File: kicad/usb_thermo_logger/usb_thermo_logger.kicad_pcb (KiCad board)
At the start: 2 copper layers, 80 x 61 mm, 50 parts, among them J1 690-005-299-043, J2 SWD, J3 RESET, J4 BOOT0, U1 STM32F070CBT6, U2 24AA02-OT, U3 MAX31855KASA, U4 MAX31855KASA, U5 PCA9531, U6 LD3985M33R_SOT23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

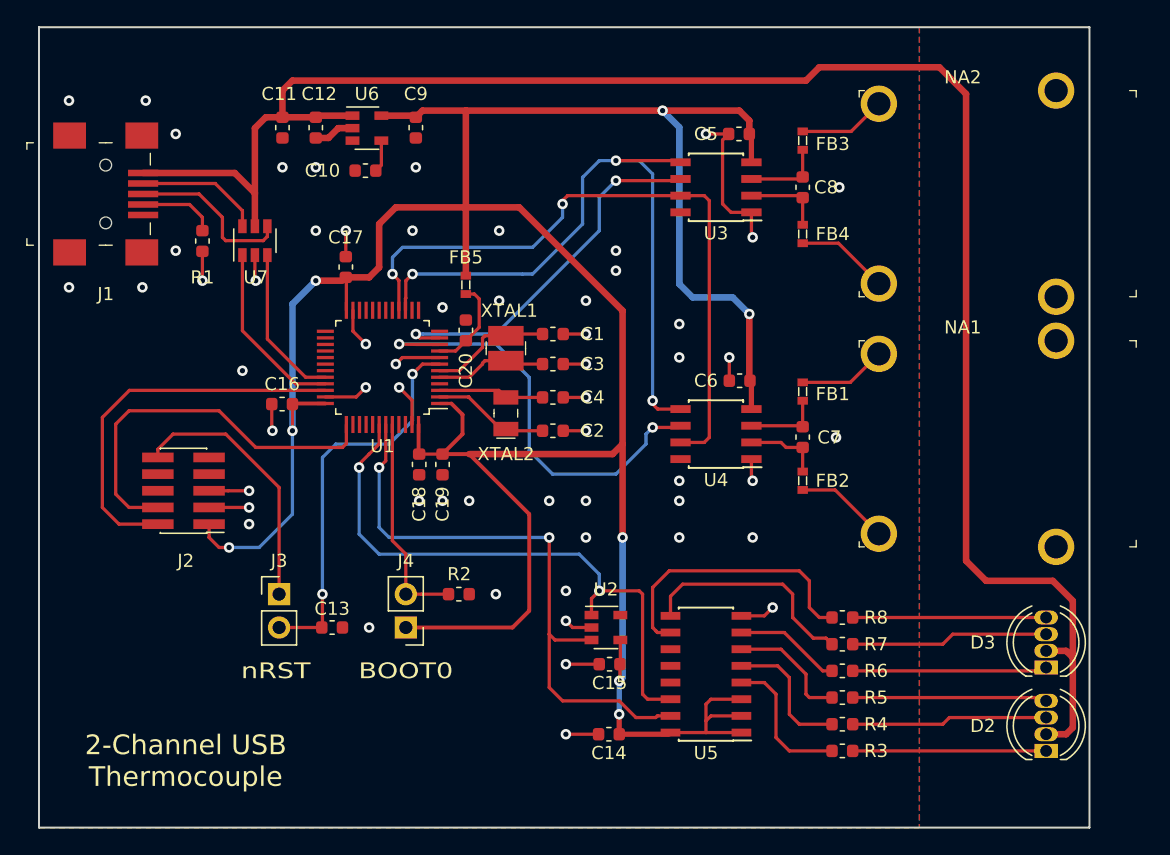
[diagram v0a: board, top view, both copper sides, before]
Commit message: LED display changes, added OpenSCAD
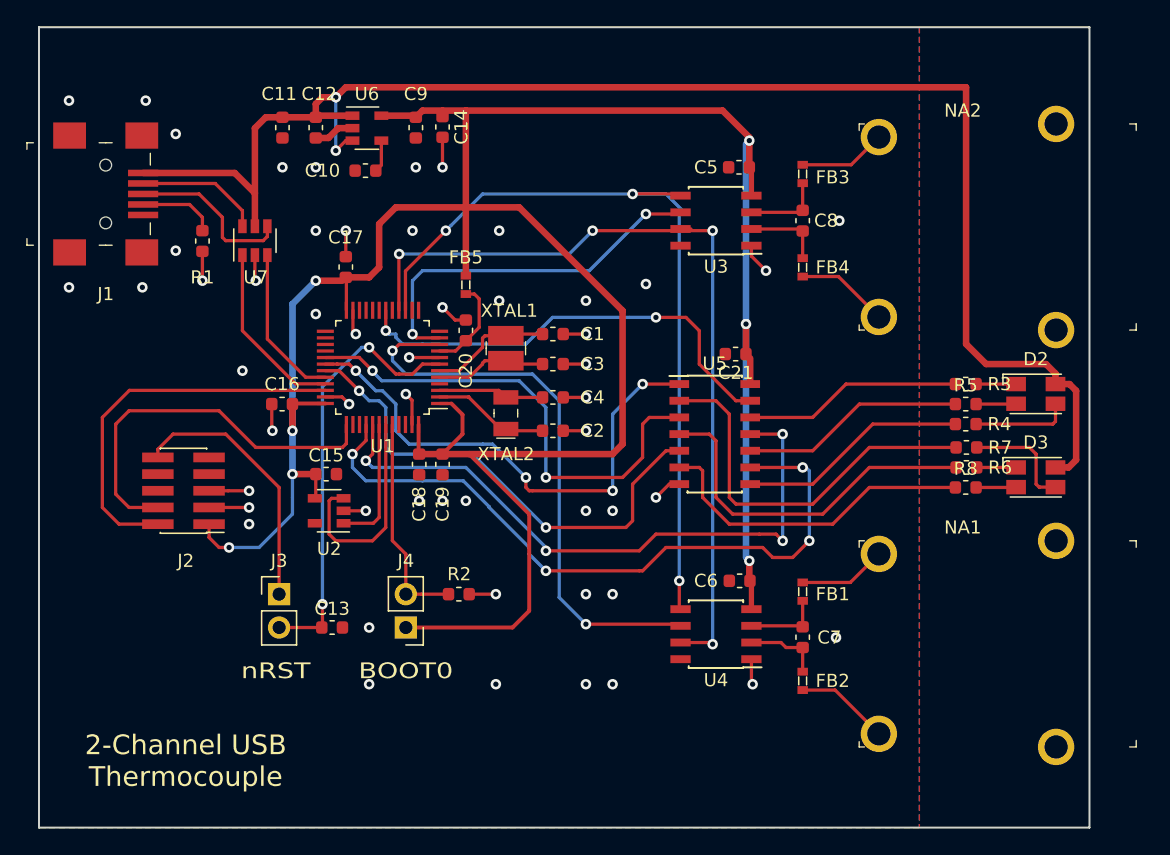
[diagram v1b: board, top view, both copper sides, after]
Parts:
- added C21: 100n, Capacitor_SMD:C_0603_1608Metric, F.Cu at (140.7, 88.4)
- D2, D3: footprint LED_THT:LED_D5.0mm-4_RGB -> LED_SMD:LED_Avago_PLCC4_3.2x2.8mm_CW
- R3, R6: value 560R -> 1k
- R4, R5, R7, R8: value 560R -> 2k2
- U5: value PCA9531 -> SN74LVC06ADR; footprint Package_SO:SOIC-16_3.9x9.9mm_P1.27mm -> Package_SO:SOIC-14_3.9x8.7mm_P1.27mm
- moved C14 48.0 mm to (118.4, 71.1), turned to 270 degrees
- moved R3 29.5 mm to (158.2, 90.7)
- moved D2 27.2 mm to (163.6, 91.4), turned to 0 degrees
- moved C15 26.0 mm to (109.5, 97.5), turned to 0 degrees
- moved R4 24.7 mm to (158.2, 93.7)
- moved R5 24.2 mm to (158.2, 92.2)
- moved U2 22.9 mm to (109.7, 100.3), turned to 180 degrees
- moved U5 18.3 mm to (139.1, 94.5), turned to 0 degrees
- moved R6 18.1 mm to (158.3, 97.0)
- moved R7 17.7 mm to (158.3, 95.5)
- moved C7 15.2 mm to (145.8, 110.0)
- moved FB2 15.2 mm to (145.8, 113.3)
- moved C6 15.2 mm to (141.0, 105.7)
- moved FB1 15.2 mm to (145.8, 106.5)
- moved NA1 15.2 mm to (165.1, 102.6)
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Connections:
- U1 pad 18: Net-(U1-Pad18) -> /RED2
- U1 pad 29: Net-(U1-Pad29) -> /RED1
- U1 pad 30: Net-(U1-Pad30) -> /GREEN1
- U1 pad 31: Net-(U1-Pad31) -> /BLUE1
- U1 pad 40: Net-(U1-Pad40) -> /GREEN2
- U1 pad 41: Net-(U1-Pad41) -> /BLUE2
- U5 pad 1: +3V3 -> /GREEN1
- U5 pad 10: Net-(R8-Pad1) -> Net-(R5-Pad1)
- U5 pad 11: Net-(U5-Pad11) -> /BLUE2
- U5 pad 12: Net-(U5-Pad12) -> Net-(R3-Pad1)
- U5 pad 13: Net-(U5-Pad13) -> /RED2
- U5 pad 14: /SCL -> +3V3
- U5 pad 2: +3V3 -> Net-(R7-Pad1)
- U5 pad 3: +3V3 -> /RED1
- U5 pad 4: Net-(R3-Pad1) -> Net-(R6-Pad1)
- U5 pad 5: Net-(R4-Pad1) -> /BLUE1
- U5 pad 6: Net-(R5-Pad1) -> Net-(R8-Pad1)
- U5 pad 7: Net-(R6-Pad1) -> GNDD
- U5 pad 8: GNDD -> Net-(R4-Pad1)
- U5 pad 9: Net-(R7-Pad1) -> /GREEN2
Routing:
- net /GREEN2: track 0.00 -> 53.6 mm, vias 0 -> 4
- net /BLUE2: track 0.00 -> 49.1 mm, vias 0 -> 4
- net /GREEN1: track 0.00 -> 39.4 mm, vias 0 -> 4
- net /BLUE1: track 0.00 -> 37.7 mm, vias 0 -> 2
- net /RED1: track 0.00 -> 37.3 mm, vias 0 -> 2
- net /SCL: track 45.2 -> 9.97 mm, vias 2 -> 0
- net /RED2: track 0.00 -> 34.8 mm, vias 0 -> 2
- net /SDA: track 46.4 -> 16.5 mm, vias 2 -> 0
- net +3V3: track 237.1 -> 213.8 mm, vias 8 -> 7
- net +5V: track 139.2 -> 118.1 mm, vias 0 -> 2
- net Net-(R6-Pad1): track 8.11 -> 27.6 mm
- net GNDD: track 62.4 -> 47.8 mm, vias 58 -> 53
- net Net-(R7-Pad1): track 17.1 -> 29.9 mm
- net Net-(D3-Pad1): track 14.8 -> 3.00 mm
- net Net-(D2-Pad4): track 14.8 -> 3.06 mm
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
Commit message: Layout changes
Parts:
- removed R1: 100k, Resistor_SMD:R_0603_1608Metric
- added TP1: SCL, TestPoint:TestPoint_Pad_1.0x1.0mm, F.Cu at (122.9, 102.6)
- added TP10: DM, TestPoint:TestPoint_Pad_1.0x1.0mm, F.Cu at (105.7, 86.1)
- added TP11: DP, TestPoint:TestPoint_Pad_1.0x1.0mm, F.Cu at (102.6, 86.1)
- added TP2: SDA, TestPoint:TestPoint_Pad_1.0x1.0mm, F.Cu at (120.1, 102.6)
- added TP3: VCC, TestPoint:TestPoint_Pad_1.0x1.0mm, F.Cu at (125.2, 72.6)
- added TP4: GND, TestPoint:TestPoint_Pad_1.0x1.0mm, F.Cu at (122.2, 72.6)
- added TP5: CS1, TestPoint:TestPoint_Pad_1.0x1.0mm, F.Cu at (131.3, 110.7)
- added TP6: SCK, TestPoint:TestPoint_Pad_1.0x1.0mm, F.Cu at (134.4, 72.6)
- added TP7: MISO, TestPoint:TestPoint_Pad_1.0x1.0mm, F.Cu at (128.3, 72.6)
- added TP8: VIN, TestPoint:TestPoint_Pad_1.0x1.0mm, F.Cu at (101.6, 70.9)
- added TP9: CS2, TestPoint:TestPoint_Pad_1.0x1.0mm, F.Cu at (131.3, 72.6)
- moved NA1 0.51 mm to (165.6, 102.6)
- moved NA2 0.51 mm to (165.6, 70.9)
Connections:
- J1 pad 2: /DP -> /DM
- J1 pad 3: /DM -> /DP
- J1 pad 4: /ID -> Net-(J1-Pad4)
- U1 pad 2: Net-(C2-Pad1) -> Net-(U1-Pad2)
- U1 pad 3: Net-(C4-Pad1) -> Net-(C2-Pad1)
- U1 pad 4: Net-(U1-Pad4) -> Net-(C4-Pad1)
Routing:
- net /SCL: track 9.97 -> 22.5 mm, vias 0 -> 2
- net /SDA: track 16.5 -> 25.2 mm, vias 0 -> 2
- net /~CS2: track 28.8 -> 36.3 mm
- net /MISO: track 63.8 -> 70.8 mm
- net /ID: track 5.94 -> 0.00 mm
- net +3V3: track 213.8 -> 218.8 mm
- net /SCK: track 61.3 -> 64.8 mm
- net +5V: track 118.1 -> 120.4 mm, vias 2 -> 4
- net GNDD: track 47.8 -> 45.6 mm
- net /~CS1: track 43.6 -> 45.4 mm
- net Net-(TP11-Pad1): track 13.8 -> 14.8 mm
- net Net-(FB4-Pad2): track 7.08 -> 7.59 mm
- net Net-(FB2-Pad2): track 7.18 -> 7.69 mm
- net Net-(FB1-Pad2): track 6.70 -> 7.21 mm
- net Net-(FB3-Pad2): track 6.68 -> 7.19 mm
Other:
- board text added: "26.06.2020 Richard Klingler"
- board text added: "SWD"
